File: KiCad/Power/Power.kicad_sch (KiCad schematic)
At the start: 54 parts, among them J1 Screw_Terminal_01x04, J2 691137710003, J3 691137710003, J4 Screw_Terminal_01x02, SW1 SW_DPST, U1 CD74HC4051E, U2 TL074, U3 L7805, U4 L7905

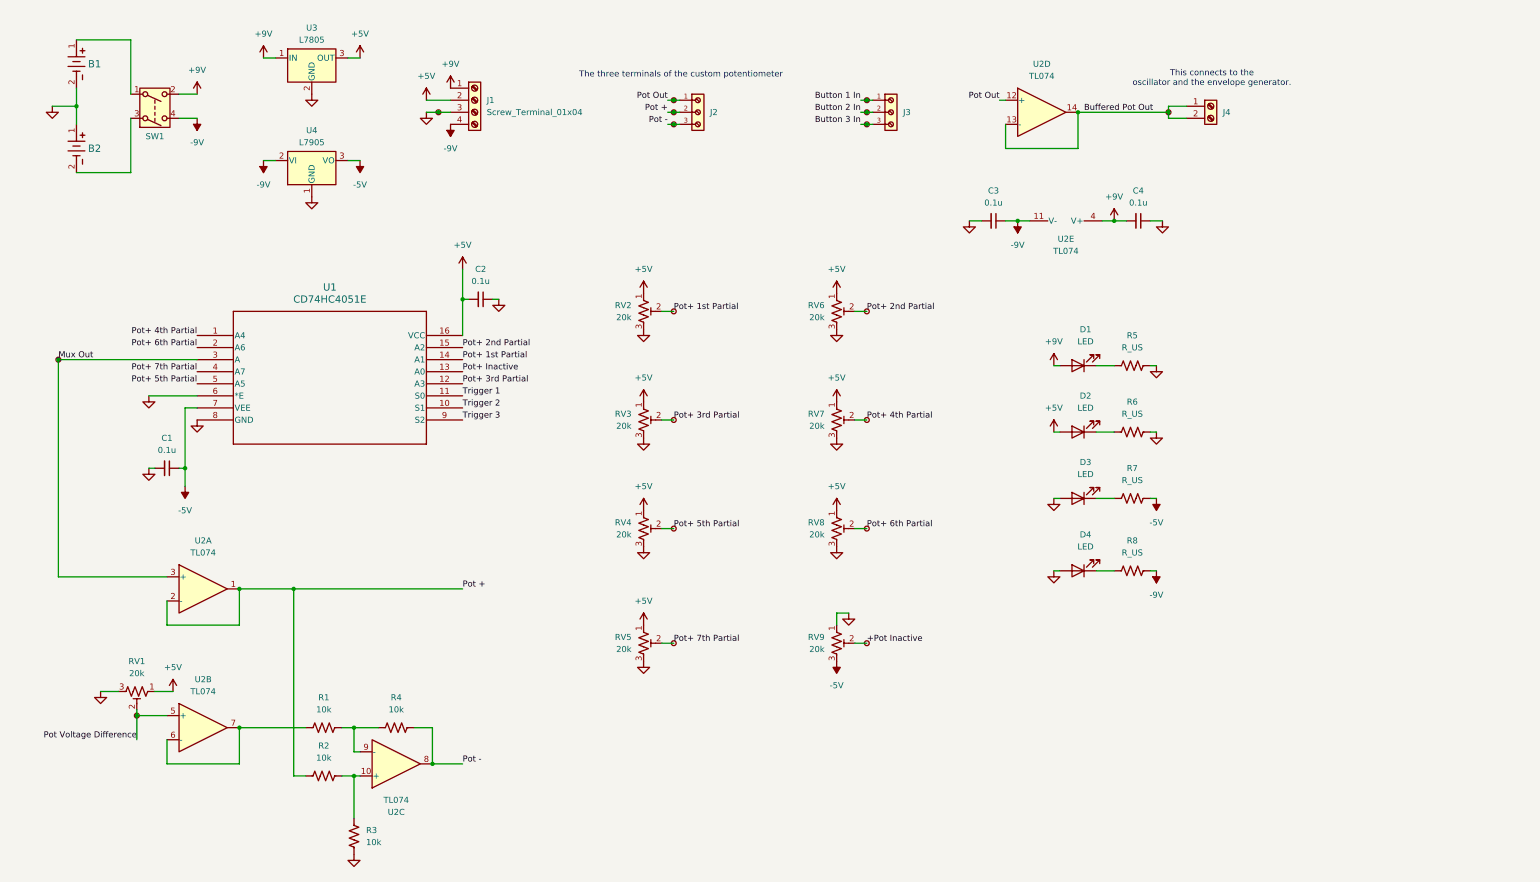
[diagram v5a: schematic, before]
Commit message: power pcb layout done
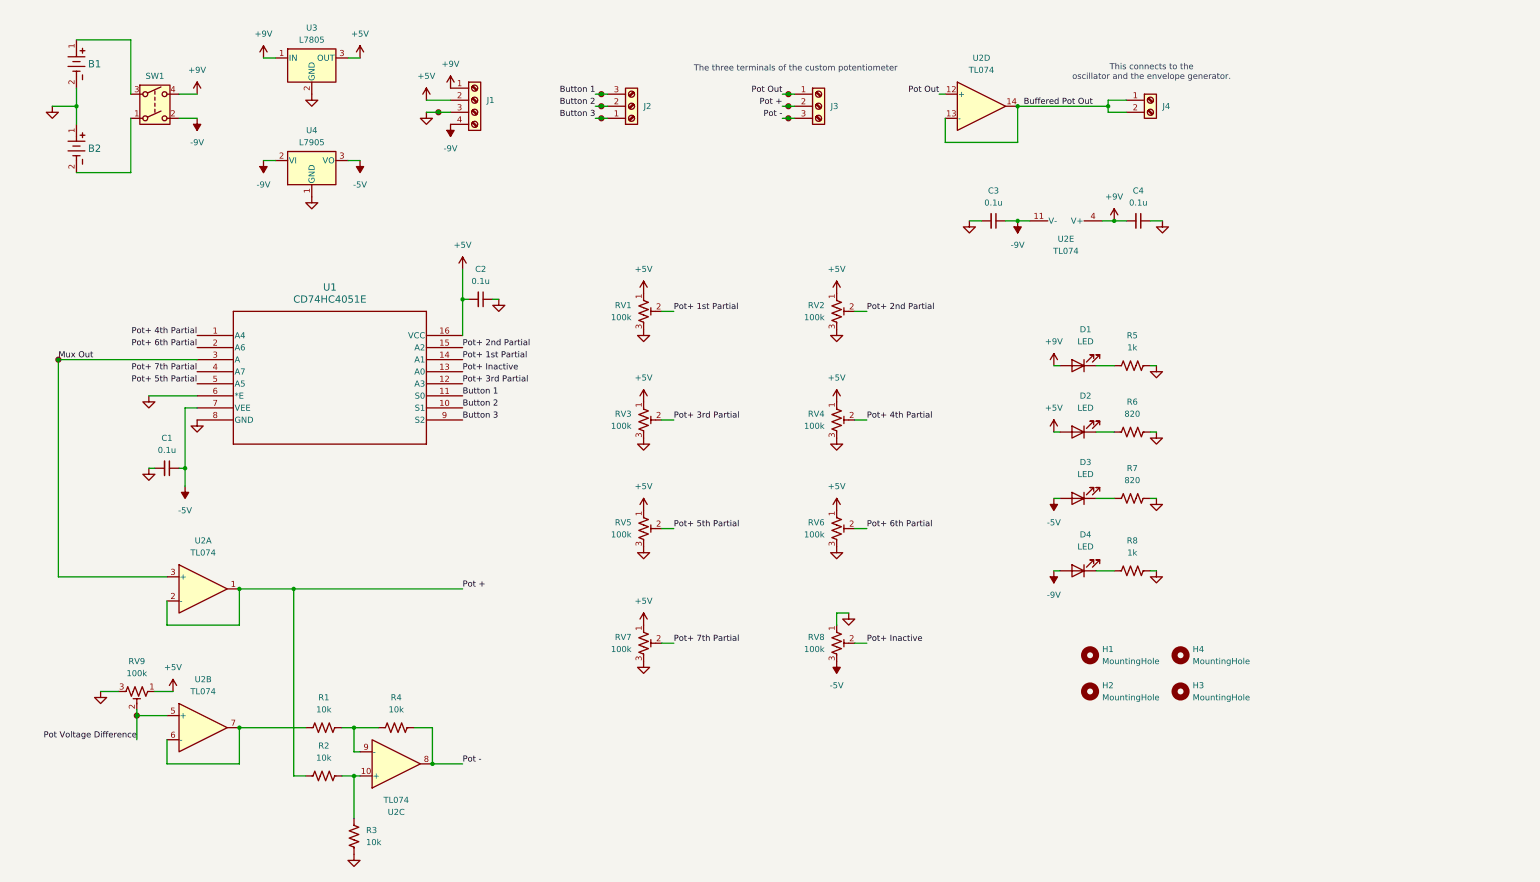
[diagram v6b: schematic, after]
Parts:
- removed J2, J3: 691137710003, Header 691137710003:691137710003, symbol Header 691137710003:691137710003
- removed TP10, TP14, TP15, TP16, TP17, TP18, TP7, TP8, TP9: TestPoint_Small, symbol Connector:TestPoint_Small
- added H1, H2, H3, H4: MountingHole, MountingHole:MountingHole_3.2mm_M3, symbol Mechanical:MountingHole
- added J2, J3: Screw_Terminal_01x03, Header 691137710003:691137710003, symbol Connector:Screw_Terminal_01x03
- C1, C2: footprint Capacitor_SMD:C_0603_1608Metric -> Capacitor_SMD:C_0805_2012Metric
- C3, C4: footprint (none) -> Capacitor_SMD:C_0805_2012Metric
- D1, D2, D3, D4: footprint (none) -> LED_THT:LED_D5.0mm
- J1: footprint (none) -> Header 691137710004:691137710004
- J4: footprint (none) -> Header 691137710002:691137710002
- R1, R2, R3, R4: footprint Resistor_SMD:R_0603_1608Metric -> Resistor_SMD:R_0805_2012Metric
- R5, R8: value R_US -> 1k; footprint (none) -> Resistor_SMD:R_0805_2012Metric
- R6, R7: value R_US -> 820; footprint (none) -> Resistor_SMD:R_0805_2012Metric
- RV1: renamed from RV2; value 20k -> 100k; footprint Potentiometer_SMD:Potentiometer_Bourns_TC33X_Vertical -> Potentiometer_THT:Potentiometer_Bourns_3339P_Vertical_HandSoldering
- RV2: renamed from RV6; value 20k -> 100k; footprint Potentiometer_SMD:Potentiometer_Bourns_TC33X_Vertical -> Potentiometer_THT:Potentiometer_Bourns_3339P_Vertical_HandSoldering
- RV3: value 20k -> 100k; footprint Potentiometer_SMD:Potentiometer_Bourns_TC33X_Vertical -> Potentiometer_THT:Potentiometer_Bourns_3339P_Vertical_HandSoldering
- RV4: renamed from RV7; value 20k -> 100k; footprint Potentiometer_SMD:Potentiometer_Bourns_TC33X_Vertical -> Potentiometer_THT:Potentiometer_Bourns_3339P_Vertical_HandSoldering
- RV5: renamed from RV4; value 20k -> 100k; footprint Potentiometer_SMD:Potentiometer_Bourns_TC33X_Vertical -> Potentiometer_THT:Potentiometer_Bourns_3339P_Vertical_HandSoldering
- RV6: renamed from RV8; value 20k -> 100k; footprint Potentiometer_SMD:Potentiometer_Bourns_TC33X_Vertical -> Potentiometer_THT:Potentiometer_Bourns_3339P_Vertical_HandSoldering
- RV7: renamed from RV5; value 20k -> 100k; footprint Potentiometer_SMD:Potentiometer_Bourns_TC33X_Vertical -> Potentiometer_THT:Potentiometer_Bourns_3339P_Vertical_HandSoldering
- RV8: renamed from RV9; value 20k -> 100k; footprint Potentiometer_SMD:Potentiometer_Bourns_TC33X_Vertical -> Potentiometer_THT:Potentiometer_Bourns_3339P_Vertical_HandSoldering
- RV9: renamed from RV1; value 20k -> 100k; footprint Potentiometer_SMD:Potentiometer_Bourns_TC33X_Vertical -> Potentiometer_THT:Potentiometer_Bourns_3339P_Vertical_HandSoldering
- SW1: footprint DPST Switch RA83231100:DPST Switch RA83231100 -> Library:DPST Switch RA83231100
- TP1, TP11, TP12, TP13, TP2, TP3, TP4, TP5, TP6: footprint (none) -> TestPoint:TestPoint_Keystone_5000-5004_Miniature
- U1: footprint Mux CD74HC4051E:N16 -> Package_DIP:DIP-16_W7.62mm
- U3, U4: footprint (none) -> Package_TO_SOT_THT:TO-220-3_Vertical
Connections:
- net +Pot Inactive is gone; now on net Pot+ Inactive: RV8.2
- net Trigger 1 is gone; now on net Button 1: U1.11 (S0)
- net Trigger 2 is gone; now on net Button 2: U1.10 (S1)
- net Trigger 3 is gone; now on net Button 3: U1.9 (S2)
- net +9V: now also SW1.4; no longer SW1.2
- net -5V: now also D3.2 (A); no longer R7.2
- net -9V: now also D4.2 (A), SW1.2; no longer R8.2, SW1.4
- net GND: now also R7.2, R8.2; no longer D3.2 (A), D4.2 (A)
- net Pot +: now also J3.2 (Pin_2)
- net Pot -: now also J3.3 (Pin_3)
- net Pot Out: now also J3.1 (Pin_1)
- net at SW1.1: now also B2.2; no longer B1.1
- net at SW1.3: now also B1.1; no longer B2.2
- net Button 1 In renamed Button 1
- net Button 1: now also J2.3 (Pin_3)
- net Button 2 In renamed Button 2
- net Button 2: now also J2.2 (Pin_2)
- net Button 3 In renamed Button 3
- net Button 3: now also J2.1 (Pin_1)
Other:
- moved on the sheet: J4, U2D

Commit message: updated power board to have more terminals
before, the power board had only one terminal for power supply, so the other boards would share this terminal. now, the power board has a terminal for each other board, so the other boards don't need to share the same terminal for power
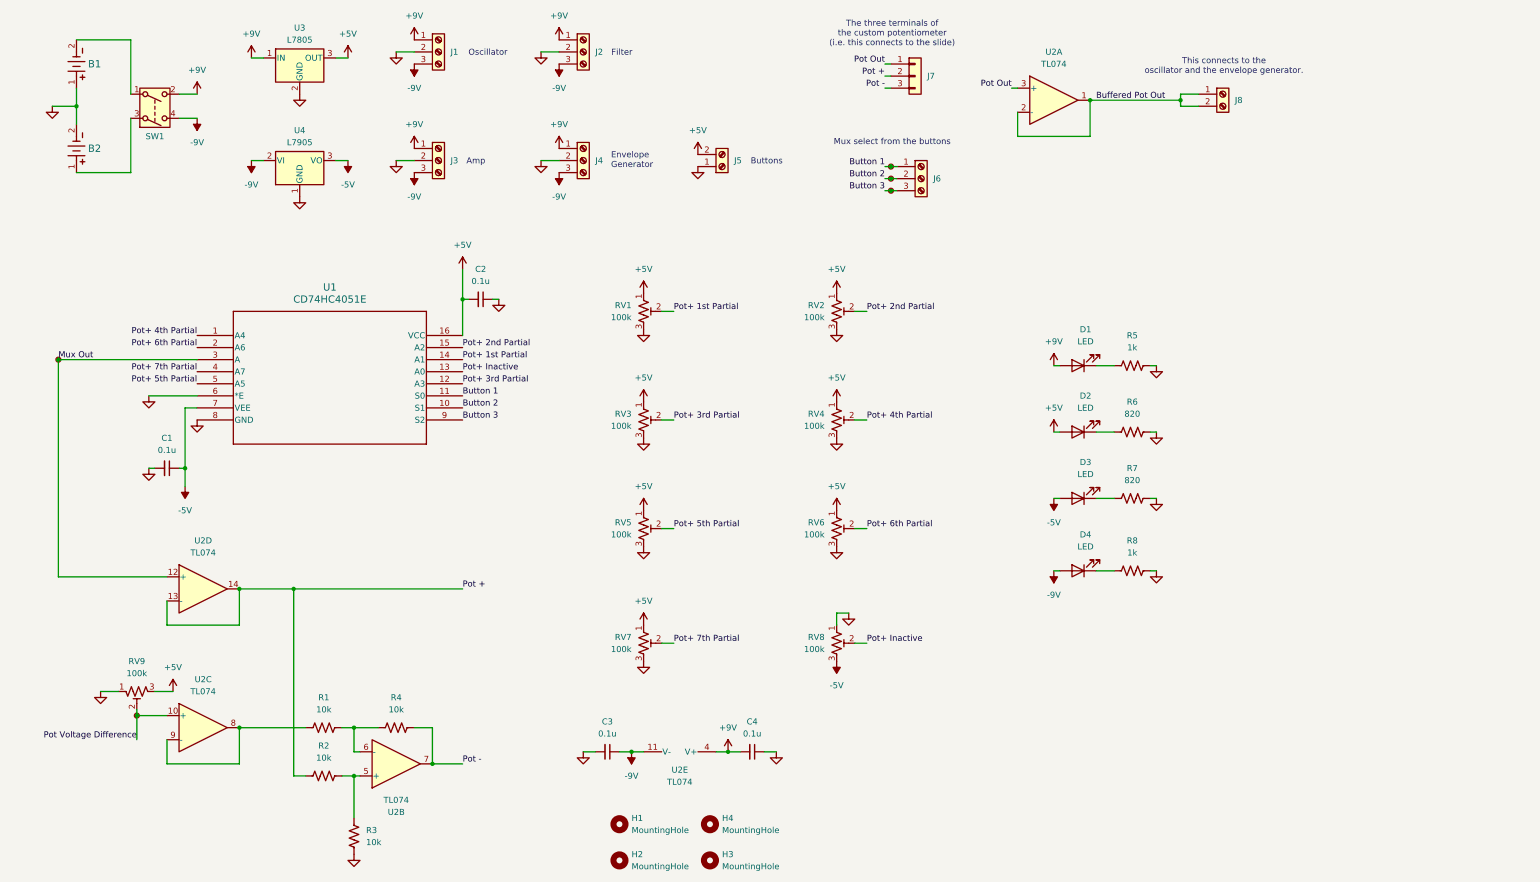
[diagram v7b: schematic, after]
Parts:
- removed J1: Screw_Terminal_01x04, Header 691137710004:691137710004, symbol Connector:Screw_Terminal_01x04
- removed TP3, TP4, TP5, TP6: TestPoint_Small, TestPoint:TestPoint_Keystone_5000-5004_Miniature, symbol Connector:TestPoint_Small
- added J1, J2, J4: Screw_Terminal_01x03, Header 691137710003:691137710003, symbol Connector:Screw_Terminal_01x03
- added J5: Screw_Terminal_01x02, Header 691137710002:691137710002, symbol Connector:Screw_Terminal_01x02
- added J7: Conn_01x03, Connector_JST:JST_XH_S3B-XH-A_1x03_P2.50mm_Horizontal, symbol Connector_Generic:Conn_01x03
- renumbered J2 to J6, J4 to J8
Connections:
- net +5V: now also RV9.3, J5.2 (Pin_2); no longer RV9.1
- net +9V: now also J3.1 (Pin_1), SW1.2, J1.1 (Pin_1), J2.1 (Pin_1), J4.1 (Pin_1); no longer SW1.4
- net -9V: now also J3.3 (Pin_3), SW1.4, J1.3 (Pin_3), J2.3 (Pin_3), J4.3 (Pin_3); no longer SW1.2
- net Buffered Pot Out: now also U2.1, U2.2 (-); no longer U2.13 (-), U2.14
- net Button 1: now also J6.1 (Pin_1); no longer J6.3 (Pin_3)
- net Button 3: now also J6.3 (Pin_3); no longer J6.1 (Pin_1)
- net GND: now also B1.1, B2.2, J3.2 (Pin_2), RV9.1, J1.2 (Pin_2), J2.2 (Pin_2), J4.2 (Pin_2), J5.1 (Pin_1); no longer B1.2, B2.1, RV9.3
- net Mux Out: now also U2.12 (+); no longer U2.3 (+)
- net Pot +: now also U2.13 (-), U2.14, J7.2 (Pin_2); no longer J3.2 (Pin_2), U2.1, U2.2 (-)
- net Pot -: now also U2.7, J7.3 (Pin_3); no longer J3.3 (Pin_3), U2.8
- net Pot Out: now also U2.3 (+), J7.1 (Pin_1); no longer J3.1 (Pin_1), U2.12 (+)
- net Pot Voltage Difference: now also U2.10 (+); no longer U2.5 (+)
- net at R2.2, R3.2: now also U2.5 (+); no longer U2.10 (+)
- net at SW1.1: now also B1.2; no longer B2.2
- net at SW1.3: now also B2.1; no longer B1.1
- net at R1.2, R4.1: now also U2.6 (-); no longer U2.9 (-)
- new net: R1.1, U2.8, U2.9 (-)
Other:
- note added: "Amp"
- note added: "Buttons"
- note added: "Envelope Generator"
- note added: "Filter"
- note added: "Mux select from the buttons"
- note added: "Oscillator"
- note added: "The three terminals of the custom potentiometer (i.e. this connects to the slide)"
- note removed: "The three terminals of the custom potentiometer"
- moved on the sheet: C3, C4, H1, H2, H3, H4, J6, J8, RV9, U2A, U2E, U3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

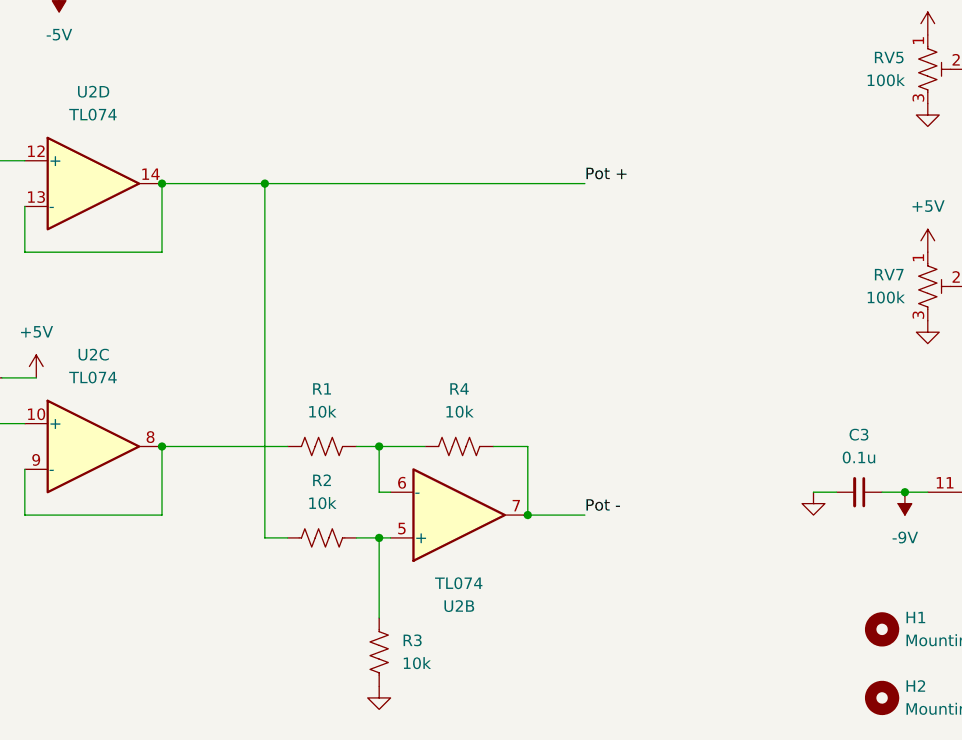
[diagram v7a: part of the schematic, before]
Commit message: added protective resistor to op amp connecting to slide pot
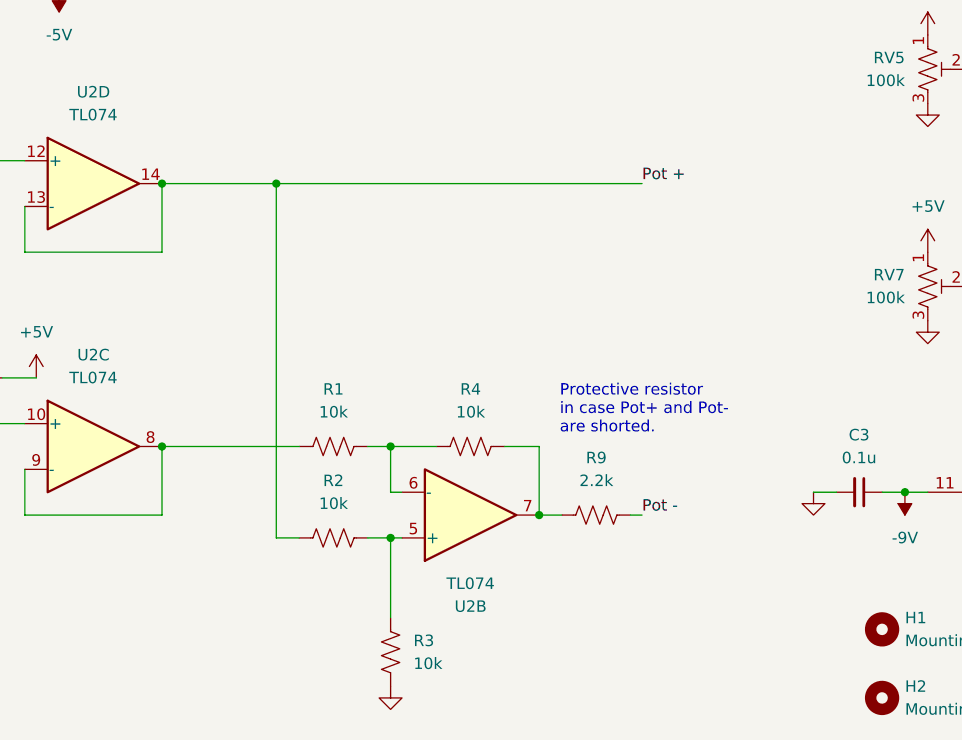
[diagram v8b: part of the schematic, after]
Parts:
- added R9: 2.2k, Resistor_SMD:R_0805_2012Metric, symbol Device:R_US
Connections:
- net Pot -: now also R9.2; no longer R4.2, U2.7
- new net: R4.2, R9.1, U2.7
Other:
- note added: "Protective resistor in case Pot+ and Pot- are shorted."
- moved on the sheet: R1, R2, R3, R4, U2B
